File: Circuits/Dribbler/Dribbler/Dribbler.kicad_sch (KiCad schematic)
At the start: 2 parts, among them J1 Dribbler_ESC, Q1 IRLB8721PBF

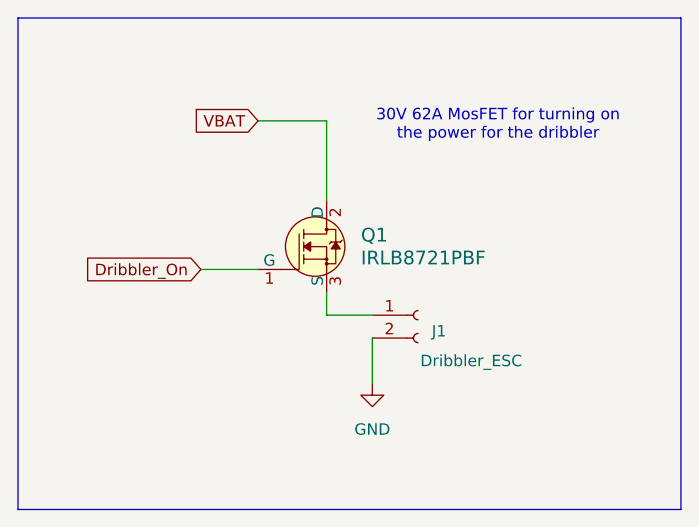
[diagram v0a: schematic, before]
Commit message: added connector for control signal
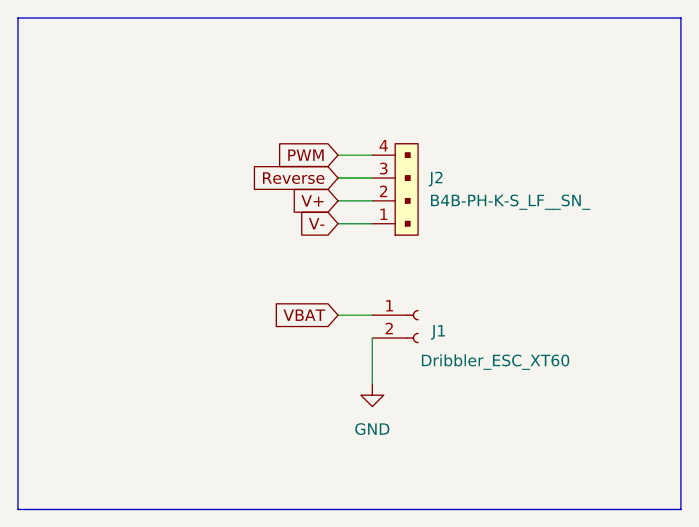
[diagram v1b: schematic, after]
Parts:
- removed Q1: IRLB8721PBF, digikey-footprints:TO-220-3, symbol dk_Transistors-FETs-MOSFETs-Single:IRLB8721PBF
- added J2: B4B-PH-K-S_LF__SN_, digikey-footprints:PinHeader_1x4_P2mm_Drill1mm, symbol dk_Rectangular-Connectors-Headers-Male-Pins:B4B-PH-K-S_LF__SN_
- J1: value Dribbler_ESC -> Dribbler_ESC_XT60
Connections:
- net VBAT: now also J1.1 (Pin_1)
- new net PWM: J2.4
- new net Reverse: J2.3
- new net V+: J2.2
- new net V-: J2.1
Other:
- note removed: "30V 62A MosFET for turning on the power for the dribbler"
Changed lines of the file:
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@@
 	(wire
 		(pts
-			(xy 49.53 34.29) (xy 57.15 34.29)
+			(xy 58.42 45.72) (xy 62.23 45.72)
+		)
+		(stroke
+			(width 0)
+			(type default)
+		)
+	)
+	(wire
+		(pts
+			(xy 58.42 55.88) (xy 62.23 55.88)
 		)
 		(stroke
@@
 	(wire
 		(pts
-			(xy 57.15 55.88) (xy 57.15 53.34)
-		)
-		(stroke
-			(width 0)
-			(type default)
-		)
-	)
-	(wire
-		(pts
-			(xy 57.15 34.29) (xy 57.15 43.18)
-		)
-		(stroke
-			(width 0)
-			(type default)
-		)
-	)
-	(wire
-		(pts
-			(xy 43.18 50.8) (xy 49.53 50.8)
-		)
-		(stroke
-			(width 0)
-			(type default)
-		)
-	)
-	(wire
-		(pts
-			(xy 57.15 55.88) (xy 62.23 55.88)
+			(xy 58.42 38.1) (xy 62.23 38.1)
+		)
+		(stroke
+			(width 0)
+			(type default)
+		)
+	)
+	(wire
+		(pts
+			(xy 58.42 40.64) (xy 62.23 40.64)
+		)
+		(stroke
+			(width 0)
+			(type default)
+		)
+	)
+	(wire
+		(pts
+			(xy 58.42 43.18) (xy 62.23 43.18)
 		)
 		(stroke
@@
 		)
 	)
-	(text "30V 62A MosFET for turning on \nthe power for the dribbler"
-		(exclude_from_sim no)
-		(at 76.2 34.798 0)
+	(global_label "PWM"
+		(shape input)
+		(at 58.42 38.1 180)
+		(fields_autoplaced yes)
 		(effects
 			(font
 				(size 1.27 1.27)
 			)
-		)
-	)
-	(global_label "Dribbler_On"
+			(justify right)
+		)
+		(property "Intersheetrefs" "${INTERSHEET_REFS}"
+			(at 51.262 38.1 0)
+			(effects
+				(font
+					(size 1.27 1.27)
+				)
+				(justify right)
+				(hide yes)
+			)
+		)
+	)
+	(global_label "V-"
 		(shape input)
-		(at 43.18 50.8 180)
+		(at 58.42 45.72 180)
 		(fields_autoplaced yes)
 		(effects
@@
 		)
 		(property "Intersheetrefs" "${INTERSHEET_REFS}"
-			(at 29.2487 50.8 0)
-			(effects
-				(font
-					(size 1.27 1.27)
-				)
-				(justify right)
-				(hide yes)
-			)
-		)
-	)
-	(global_label "VBAT"
+			(at 52.7738 45.72 0)
+			(effects
+				(font
+					(size 1.27 1.27)
+				)
+				(justify right)
+				(hide yes)
+			)
+		)
+	)
+	(global_label "V+"
 		(shape input)
-		(at 49.53 34.29 180)
+		(at 58.42 43.18 180)
 		(fields_autoplaced yes)
 		(effects
@@
 		)
 		(property "Intersheetrefs" "${INTERSHEET_REFS}"
-			(at 42.13 34.29 0)
+			(at 52.7738 43.18 0)
+			(effects
+				(font
+					(size 1.27 1.27)
+				)
+				(justify right)
+				(hide yes)
+			)
+		)
+	)
+	(global_label "VBAT"
+		(shape input)
+		(at 58.42 55.88 180)
+		(fields_autoplaced yes)
+		(effects
+			(font
+				(size 1.27 1.27)
+			)
+			(justify right)
+		)
+		(property "Intersheetrefs" "${INTERSHEET_REFS}"
+			(at 51.02 55.88 0)
+			(effects
+				(font
+					(size 1.27 1.27)
+				)
+				(justify right)
+				(hide yes)
+			)
+		)
+	)
+	(global_label "Reverse"
+		(shape input)
+		(at 58.42 40.64 180)
+		(fields_autoplaced yes)
+		(effects
+			(font
+				(size 1.27 1.27)
+			)
+			(justify right)
+		)
+		(property "Intersheetrefs" "${INTERSHEET_REFS}"
+			(at 48.1171 40.64 0)
 			(effects
 				(font
@@
 			)
 		)
-		(property "Value" "Dribbler_ESC"
+		(property "Value" "Dribbler_ESC_XT60"
 			(at 67.564 60.96 0)
 			(effects
@@
 	)
 	(symbol
-		(lib_id "dk_Transistors-FETs-MOSFETs-Single:IRLB8721PBF")
-		(at 57.15 48.26 0)
+		(lib_id "dk_Rectangular-Connectors-Headers-Male-Pins:B4B-PH-K-S_LF__SN_")
+		(at 64.77 45.72 90)
 		(unit 1)
 		(exclude_from_sim no)
@@
 		(dnp no)
 		(fields_autoplaced yes)
-		(property "Reference" "Q1"
-			(at 60.96 46.9899 0)
-			(effects
-				(font
-					(size 1.524 1.524)
-				)
-				(justify left)
-			)
-		)
-		(property "Value" "IRLB8721PBF"
-			(at 60.96 49.5299 0)
-			(effects
-				(font
-					(size 1.524 1.524)
-				)
-				(justify left)
-			)
-		)
-		(property "Footprint" "digikey-footprints:TO-220-3"
-			(at 62.23 43.18 0)
-			(effects
-				(font
-					(size 1.524 1.524)
-				)
-				(justify left)
-				(hide yes)
-			)
-		)
-		(property "Datasheet" "https://www.infineon.com/dgdl/irlb8721pbf.pdf?fileId=5546d462533600a40153566056732591"
-			(at 62.23 40.64 0)
-			(effects
-				(font
-					(size 1.524 1.524)
-				)
-				(justify left)
-				(hide yes)
-			)
-		)
-		(property "Description" "MOSFET N-CH 30V 62A TO-220AB"
-			(at 57.15 48.26 0)
-			(effects
-				(font
-					(size 1.27 1.27)
-				)
-				(hide yes)
-			)
-		)
-		(property "Digi-Key_PN" "IRLB8721PBF-ND"
-			(at 62.23 38.1 0)
-			(effects
-				(font
-					(size 1.524 1.524)
-				)
-				(justify left)
-				(hide yes)
-			)
-		)
-		(property "MPN" "IRLB8721PBF"
-			(at 62.23 35.56 0)
-			(effects
-				(font
-					(size 1.524 1.524)
-				)
-				(justify left)
-				(hide yes)
-			)
-		)
-		(property "Category" "Discrete Semiconductor Products"
-			(at 62.23 33.02 0)
-			(effects
-				(font
-					(size 1.524 1.524)
-				)
-				(justify left)
-				(hide yes)
-			)
-		)
-		(property "Family" "Transistors - FETs, MOSFETs - Single"
-			(at 62.23 30.48 0)
-			(effects
-				(font
-					(size 1.524 1.524)
-				)
-				(justify left)
-				(hide yes)
-			)
-		)
-		(property "DK_Datasheet_Link" "https://www.infineon.com/dgdl/irlb8721pbf.pdf?fileId=5546d462533600a40153566056732591"
-			(at 62.23 27.94 0)
-			(effects
-				(font
-					(size 1.524 1.524)
-				)
-				(justify left)
-				(hide yes)
-			)
-		)
-		(property "DK_Detail_Page" "/product-detail/en/infineon-technologies/IRLB8721PBF/IRLB8721PBF-ND/2127670"
-			(at 62.23 25.4 0)
-			(effects
-				(font
-					(size 1.524 1.524)
-				)
-				(justify left)
-				(hide yes)
-			)
-		)
-		(property "Description_1" "MOSFET N-CH 30V 62A TO-220AB"
-			(at 62.23 22.86 0)
-			(effects
-				(font
-					(size 1.524 1.524)
-				)
-				(justify left)
-				(hide yes)
-			)
-		)
-		(property "Manufacturer" "Infineon Technologies"
-			(at 62.23 20.32 0)
+		(property "Reference" "J2"
+			(at 68.58 40.6399 90)
+			(effects
+				(font
+					(size 1.27 1.27)
+				)
+				(justify right)
+			)
+		)
+		(property "Value" "B4B-PH-K-S_LF__SN_"
+			(at 68.58 43.1799 90)
+			(effects
+				(font
+					(size 1.27 1.27)
+				)
+				(justify right)
+			)
+		)
+		(property "Footprint" "digikey-footprints:PinHeader_1x4_P2mm_Drill1mm"
+			(at 59.69 40.64 0)
+			(effects
+				(font
+					(size 1.524 1.524)
+				)
+				(justify left)
+				(hide yes)
+			)
+		)
+		(property "Datasheet" "http://www.jst-mfg.com/product/pdf/eng/ePH.pdf"
+			(at 57.15 40.64 0)
+			(effects
+				(font
+					(size 1.524 1.524)
+				)
+				(justify left)
+				(hide yes)
+			)
+		)
+		(property "Description" "CONN HEADER VERT 4POS 2MM"
+			(at 64.77 45.72 0)
+			(effects
+				(font
+					(size 1.27 1.27)
+				)
+				(hide yes)
+			)
+		)
+		(property "Digi-Key_PN" "455-1706-ND"
+			(at 54.61 40.64 0)
+			(effects
+				(font
+					(size 1.524 1.524)
+				)
+				(justify left)
+				(hide yes)
+			)
+		)
+		(property "MPN" "B4B-PH-K-S(LF)(SN)"
+			(at 52.07 40.64 0)
+			(effects
+				(font
+					(size 1.524 1.524)
+				)
+				(justify left)
+				(hide yes)
+			)
+		)
+		(property "Category" "Connectors, Interconnects"
+			(at 49.53 40.64 0)
+			(effects
+				(font
+					(size 1.524 1.524)
+				)
+				(justify left)
+				(hide yes)
+			)
+		)
+		(property "Family" "Rectangular Connectors - Headers, Male Pins"
+			(at 46.99 40.64 0)
+			(effects
+				(font
+					(size 1.524 1.524)
+				)
+				(justify left)
+				(hide yes)
+			)
+		)
+		(property "DK_Datasheet_Link" "http://www.jst-mfg.com/product/pdf/eng/ePH.pdf"
+			(at 44.45 40.64 0)
+			(effects
+				(font
+					(size 1.524 1.524)
+				)
+				(justify left)
+				(hide yes)
+			)
+		)
+		(property "DK_Detail_Page" "/product-detail/en/jst-sales-america-inc/B4B-PH-K-S(LF)(SN)/455-1706-ND/926613"
+			(at 41.91 40.64 0)
+			(effects
+				(font
+					(size 1.524 1.524)
+				)
+				(justify left)
+				(hide yes)
+			)
+		)
+		(property "Description_1" "CONN HEADER VERT 4POS 2MM"
+			(at 39.37 40.64 0)
+			(effects
+				(font
+					(size 1.524 1.524)
+				)
+				(justify left)
+				(hide yes)
+			)
+		)
+		(property "Manufacturer" "JST Sales America Inc."
+			(at 36.83 40.64 0)
 			(effects
 				(font
@@
 		)
 		(property "Status" "Active"
-			(at 62.23 17.78 0)
-			(effects
-				(font
-					(size 1.524 1.524)
-				)
-				(justify left)
-				(hide yes)
-			)
+			(at 34.29 40.64 0)
+			(effects
+				(font
+					(size 1.524 1.524)
+				)
+				(justify left)
+				(hide yes)
+			)
+		)
+		(pin "3"
 		)
 		(pin "2"
@@
 		(pin "1"
 		)
-		(pin "3"
+		(pin "4"
 		)
 		(instances
 			(project ""
 				(path "/ec51de40-29d4-4d77-b10b-52a3fd594a69"
-					(reference "Q1")
+					(reference "J2")
 					(unit 1)
 				)
